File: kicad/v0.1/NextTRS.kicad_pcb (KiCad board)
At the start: 2 copper layers, 145.7 x 107.8 mm, 98 parts, among them J1 TRS-80 M3 Pin Header, J10 AudioJack3, J11 Mini-DIN-6, J12 USB_B_Micro, J2 TRS-80 M1 Pin Connector, J3 TRS-80 M3 Edge Connector, J4 TRS-80 M1 Edge Connector, J5 Conn_01x06_Male, J6 Conn_01x06_Male, J7 HDMI_A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

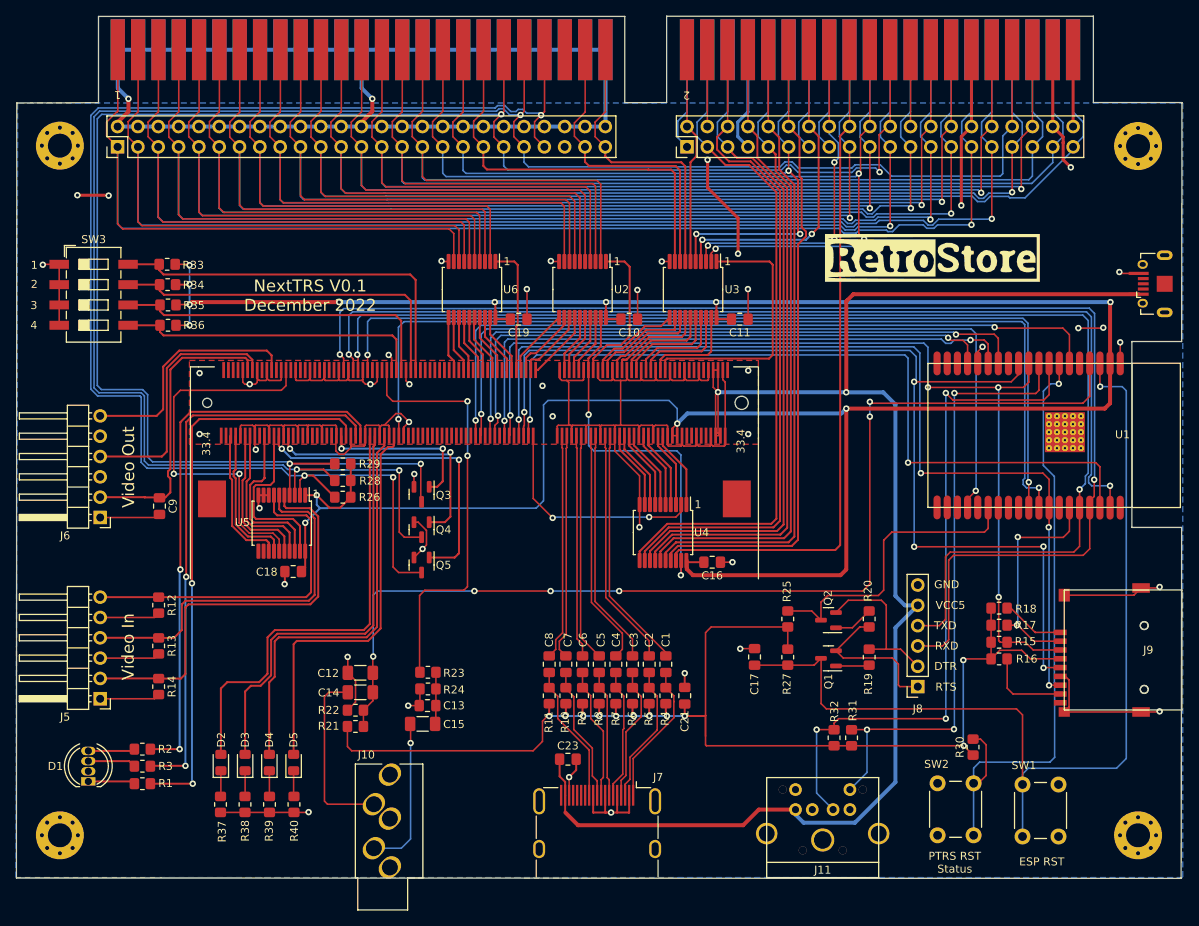
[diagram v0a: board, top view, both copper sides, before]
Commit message: Move micro-USB connector closer to edge
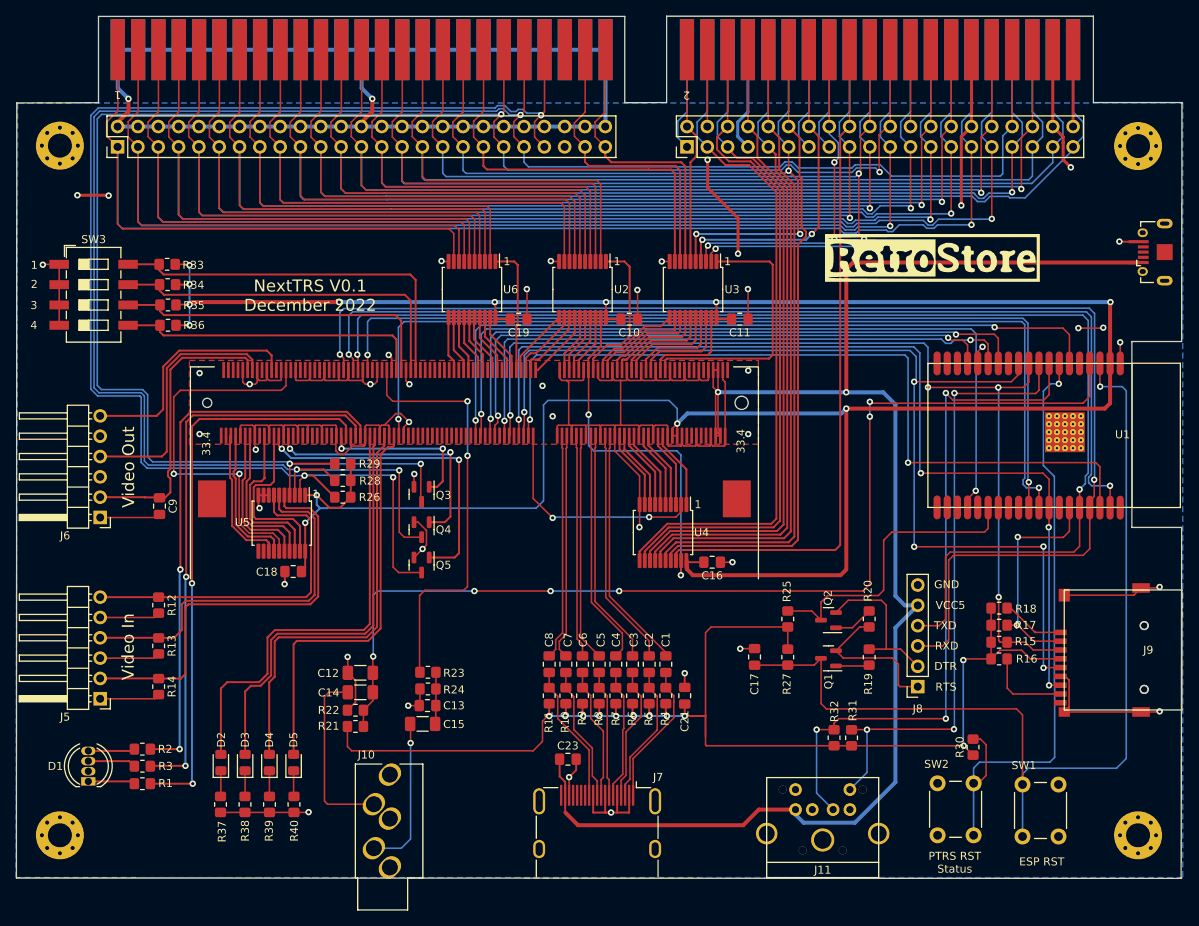
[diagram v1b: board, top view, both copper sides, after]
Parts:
- moved J12 3.96 mm to (164.8, 74.7)
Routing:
- net +5V: track 192.5 -> 196.5 mm
